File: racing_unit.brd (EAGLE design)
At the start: 81 x 80 mm, 56 parts, among them IC1 78L05Z, IC2 78L05Z, IC3 78L05Z, IC4 78L05Z, J1 J10MM, J2 J10MM, J3 J5MM, J4 J5MM, J5 J7MM, J6 J7MM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

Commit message: fixed pcb
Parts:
- removed J6: J7MM, jumper:07
- moved R6 23.9 mm to (51.4, 31.8), turned to 0 degrees
- moved R1 23.4 mm to (14.0, 30.5), turned to 270 degrees
- moved R2 23.4 mm to (16.5, 30.5), turned to 270 degrees
- moved R3 23.4 mm to (21.6, 30.5), turned to 270 degrees
- moved R4 23.4 mm to (24.1, 30.5), turned to 270 degrees
- moved HC-06 23.3 mm to (72.4, 42.5), turned to 180 degrees
- moved J4 21.7 mm to (43.2, 18.7), turned to 90 degrees
- moved R5 21.3 mm to (44.5, 31.8), turned to 180 degrees
- moved R14 18.8 mm to (26.7, 6.99), turned to 0 degrees
- moved MPU6050 18.8 mm to (47.6, 17.8), turned to 270 degrees
- moved ARDUINO_13-24 18.5 mm to (27.9, 10.2)
- moved SUPPLY 17.8 mm to (52.1, 74.9)
- moved R7 15.5 mm to (34.3, 21.6), turned to 0 degrees
- moved ARDUINI_1-12 13.7 mm to (27.9, 25.4)
- moved J5 12.2 mm to (38.7, 17.8)
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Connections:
- removed net N$31 (its old number): ARDUINI_1-12.11, J4.2, R2.2
- removed net N$34: ARDUINI_1-12.8, J6.2, R4.2
- new net N$18: ARDUINO_13-24.4, J5.2, QS_SENSOR.2, R8.2
- net N$20: now also J3.1; no longer MPU6050.8
- net N$27: now also J4.1; no longer MPU6050.3
- net N$28: now also ARDUINI_1-12.12, R1.2; no longer J3.2
- net N$29: now also J3.2, MPU6050.8; no longer ARDUINI_1-12.12, J3.1, R1.2
- net N$33: now also J4.2, MPU6050.3; no longer ARDUINI_1-12.9, J5.2, R3.2
- net N$35: now also ARDUINI_1-12.11, R2.2; no longer J4.1
- net N$38: now also ARDUINI_1-12.9, R3.2; no longer J5.1
- net N$41: now also ARDUINI_1-12.8, R4.2; no longer J6.1
- net N$5: now also J5.1; no longer ARDUINO_13-24.4, QS_SENSOR.2, R8.2
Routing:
- net GND: track 0.64 -> 379.1 mm
- net N$5: track 167.9 -> 71.5 mm
- net N$29: track 8.25 -> 68.9 mm
- net N$20: track 57.7 -> 5.87 mm
- net N$18: track 0.00 -> 45.7 mm
- net N$19: track 78.7 -> 114.7 mm
- net N$24: track 13.2 -> 39.6 mm
- net N$27: track 50.5 -> 24.4 mm
- net N$6: track 19.7 -> 45.4 mm
- net N$25: track 17.4 -> 37.8 mm
- net N$23: track 17.4 -> 36.4 mm
- net N$16: track 42.8 -> 26.0 mm
- net N$31: track 33.9 -> 20.7 mm
- net N$26: track 37.8 -> 50.9 mm
- net N$31 (its old number): track 8.25 -> 0.00 mm
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
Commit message: updated pcb and schematic
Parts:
- J3: value J5MM -> J10MM; device jumper:05 -> jumper:10
- moved QS_SENSOR 98.6 mm to (61.0, 92.7), turned to 180 degrees
- moved C2 43.1 mm to (36.8, 79.4), turned to 180 degrees
- moved C1 19.3 mm to (54.0, 79.4), turned to 180 degrees
- moved COIL1 17.8 mm to (10.2, 92.7)
- moved COIL2 17.8 mm to (20.3, 92.7)
- moved COIL3 17.8 mm to (30.5, 92.7)
- moved COIL4 17.8 mm to (40.6, 92.7)
- moved SUPPLY 17.8 mm to (50.8, 92.7)
- moved HC-06 8.28 mm to (65.4, 38.1)
- moved J3 8.03 mm to (12.1, 12.7)
- moved J4 1.85 mm to (42.2, 17.1)
- moved J5 1.42 mm to (40.0, 18.4)
- moved Q1 1.27 mm to (8.89, 62.2)
- moved Q2 1.27 mm to (24.1, 62.2)
- moved D4 1.27 mm to (58.4, 43.2)
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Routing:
- net N$18: track 45.7 -> 206.3 mm
- net N$16: track 26.0 -> 184.2 mm
- net N$4: track 28.3 -> 68.3 mm
- net N$9: track 21.8 -> 59.6 mm
- net N$3: track 26.8 -> 59.1 mm
- net N$10: track 19.3 -> 48.9 mm
- net N$19: track 114.7 -> 140.3 mm
- net N$2: track 25.5 -> 49.1 mm
- net N$11: track 17.2 -> 38.8 mm
- net N$29: track 68.9 -> 48.3 mm
- net GND: track 379.1 -> 398.7 mm
- net N$12: track 15.8 -> 33.4 mm
- net N$1: track 26.6 -> 42.3 mm
- net N$5: track 71.5 -> 59.0 mm
- net N$6: track 45.4 -> 37.0 mm
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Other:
- board size 81 x 80 mm -> 75.2 x 98.1 mm
- board text added: "Racing Unit"

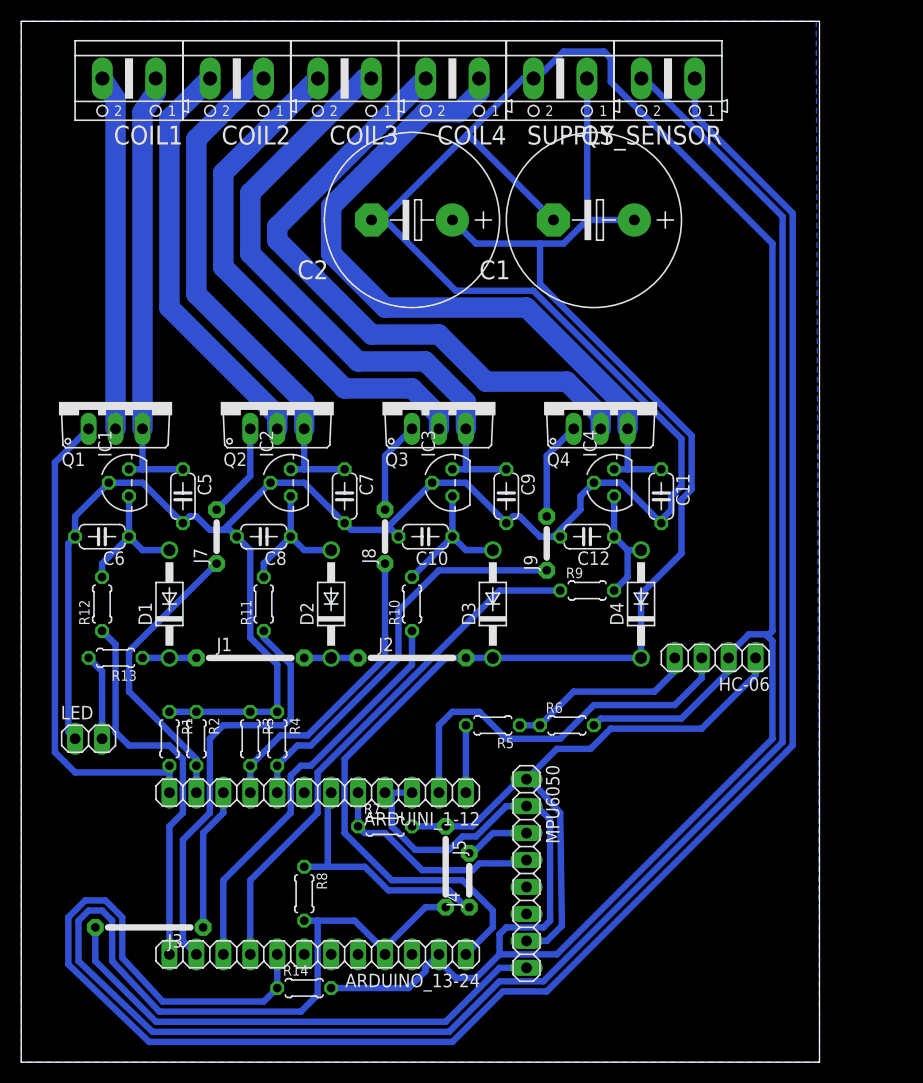
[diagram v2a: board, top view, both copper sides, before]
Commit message: updated pcb and improved spark killing procedure
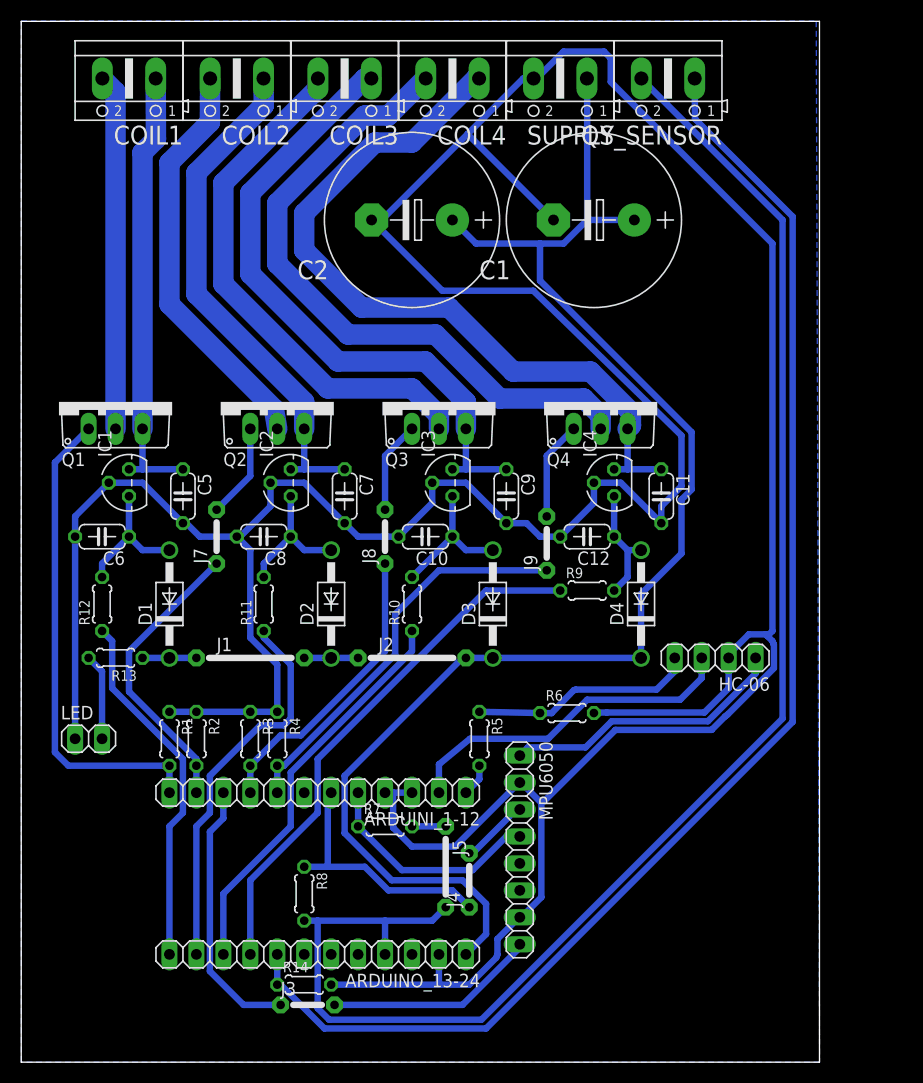
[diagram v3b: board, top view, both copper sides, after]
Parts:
- J3: value J10MM -> J5MM; device jumper:10 -> jumper:05
- moved J3 16.6 mm to (27.0, 5.40), turned to 0 degrees
- moved MPU6050 2.31 mm to (47.0, 20.0)
- moved R5 1.80 mm to (43.2, 30.5), turned to 270 degrees
- moved R6 1.16 mm to (51.4, 32.9)
- moved R14 0.32 mm to (26.7, 7.30)
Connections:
- removed net N$5: HC-06.1, J5.1, MPU6050.1, MPU6050.7, R7.2
- new net N$34: HC-06.1, MPU6050.1
- new net N$36: J5.1, R7.2
- net GND: now also MPU6050.7
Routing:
- net N$18: track 206.3 -> 147.1 mm
- net N$5: track 59.0 -> 0.00 mm
- net N$16: track 184.2 -> 129.7 mm
- net N$29: track 48.3 -> 20.0 mm
- net N$34: track 0.00 -> 26.9 mm
- net GND: track 398.7 -> 383.9 mm
- net N$20: track 13.5 -> 25.3 mm
- net N$6: track 37.0 -> 32.6 mm
- net N$4: track 68.3 -> 72.3 mm
- net N$32: track 18.0 -> 21.3 mm
- net N$22: track 6.35 -> 3.07 mm
- net N$36: track 0.00 -> 3.18 mm
- net N$24: track 39.6 -> 36.5 mm
- net N$9: track 59.6 -> 62.2 mm
- net N$23: track 36.4 -> 34.2 mm
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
